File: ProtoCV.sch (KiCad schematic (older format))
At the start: 2 parts

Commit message: Draft schematic.
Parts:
- removed U?: DC80508Z, symbol Local:DC80508Z
- removed U?: IPS240x240, symbol Local:IPS240x240
- added C1, C10, C2, C3, C4, C7, C8, C9: 22p, symbol Device:C
- added C11, C12, C13, C15, C5, C6: 100n, symbol Device:C
- added C14: 1u, symbol Device:C
- added C16, C19, C20: 22u, Capacitor_SMD:C_1206_3216Metric, symbol Device:C
- added C17, C18: 22u, Capacitor_SMD:CP_Elec_5x5.4, symbol Device:CP
- added C21, C22, C23, C24, C27, C28: 100n, Capacitor_SMD:C_0603_1608Metric, symbol Device:C
- added C25, C26: 10u, Capacitor_SMD:CP_Elec_4x5.8, symbol Device:CP
- added D1, D2: DFLR1400-7, Diode_SMD:D_PowerDI-123, symbol Device:D
- added D3: LED, LED_SMD:LED_0603_1608Metric_Castellated, symbol Device:LED
- added FB1, FB2, FB3: Ferrite_Bead, Inductor_SMD:L_0603_1608Metric, symbol Device:Ferrite_Bead
- added H1, H2, H3, H4: MountingHole, symbol Mechanical:MountingHole
- added J1, J2, J3, J4, J5, J6, J7, J8: AudioJack2_SwitchT, symbol Connector:AudioJack2_SwitchT
- added J10: Conn_01x09_Male, symbol Connector:Conn_01x09_Male
- added J11: Conn_01x05_Male, symbol Connector:Conn_01x05_Male
- added J9: Conn_02x05_Odd_Even, Connector_PinHeader_2.54mm:PinHeader_2x05_P2.54mm_Vertical, symbol Connector_Generic:Conn_02x05_Odd_Even
- added L1: 33u, Inductor_SMD:L_0805_2012Metric, symbol pspice:INDUCTOR
- added R1, R13, R14, R15, R16, R2, R3, R4: 24k9, symbol Device:R
- added R10, R11, R12, R21, R22, R23, R24, R9: 220, symbol Device:R
- added R17, R18, R19, R20, R5, R6, R7, R8: 100k, symbol Device:R
- added R25, R26: 4k7, symbol Device:R
- added R27: 1k, Resistor_SMD:R_0603_1608Metric, symbol Device:R
- added U1, U2: OPA4192, symbol Amplifier_Operational:LM324A
- added U3: DC80508Z, symbol Local:DC80508Z
- added U4: R-78E3.3-0.5, Converter_DCDC:Converter_DCDC_RECOM_R-78E-0.5_THT, symbol Regulator_Switching:R-78E3.3-0.5
- added U5: LD2981ABU33TR, Package_TO_SOT_SMD:SOT-89-3, symbol Local:LD2981ABU33TR
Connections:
- net labels added: +12V, +3.3V, +3.3VA, -12V, BIAS, CV0, CV1, CV2, CV3, CV4, CV5, CV6, CV7, GND, OUT0, OUT1, OUT2, OUT3, OUT4, OUT5, OUT6, OUT7, VREF
- wire segments 0 -> 286
- no-connect marks 0 -> 8

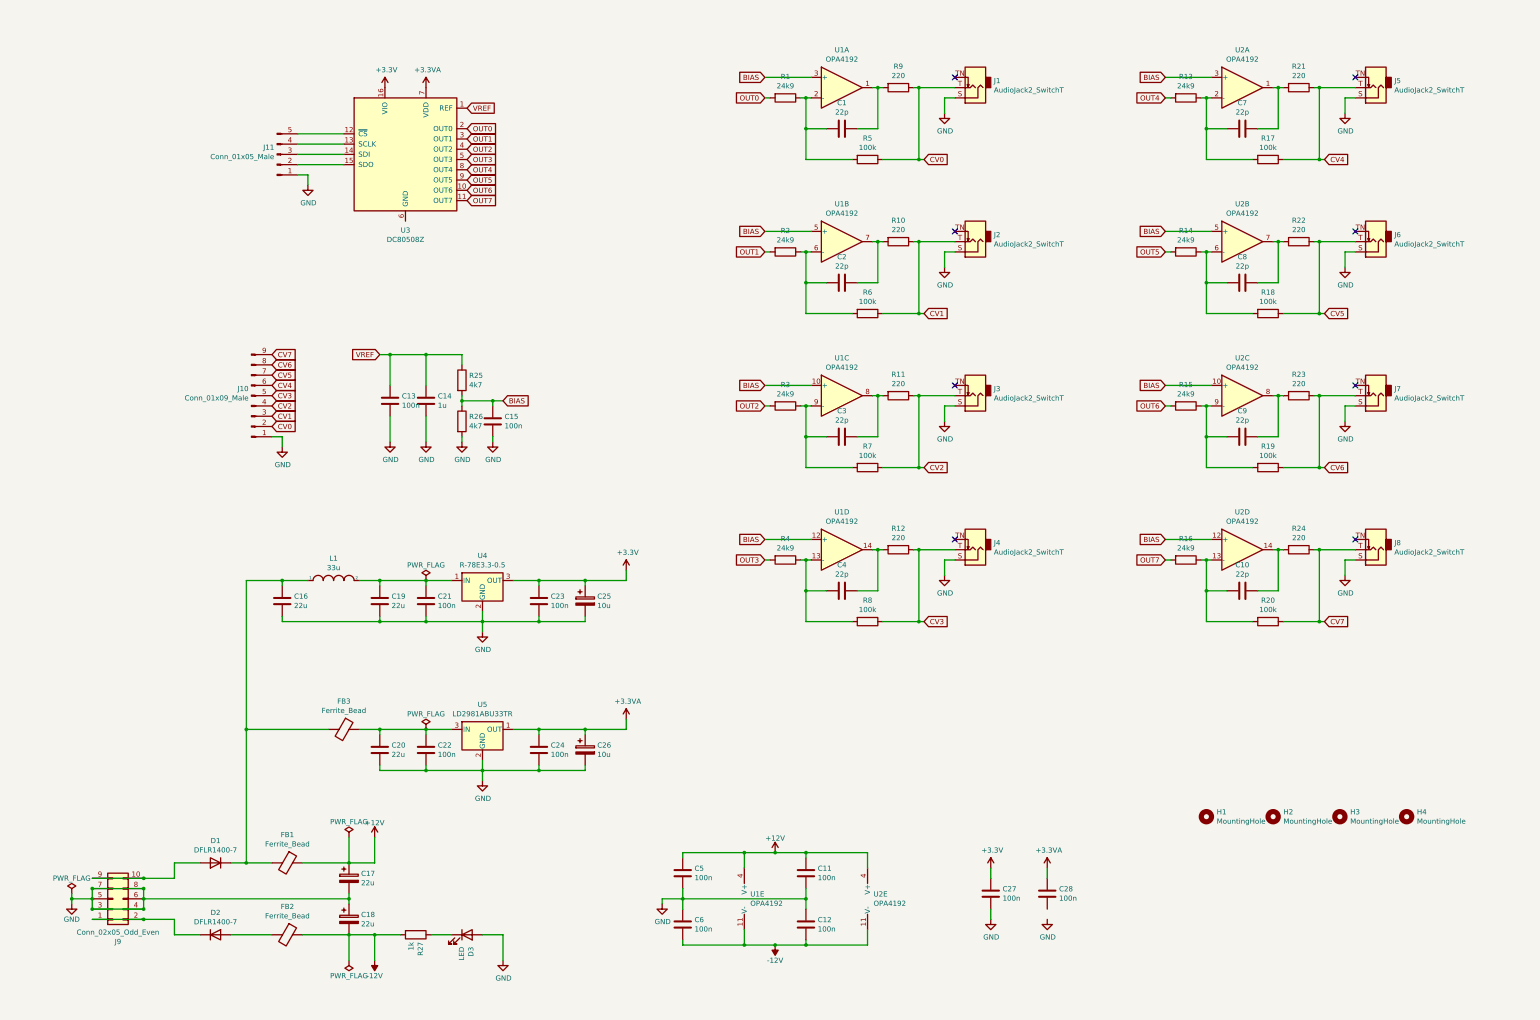
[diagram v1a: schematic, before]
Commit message: Added triggers.
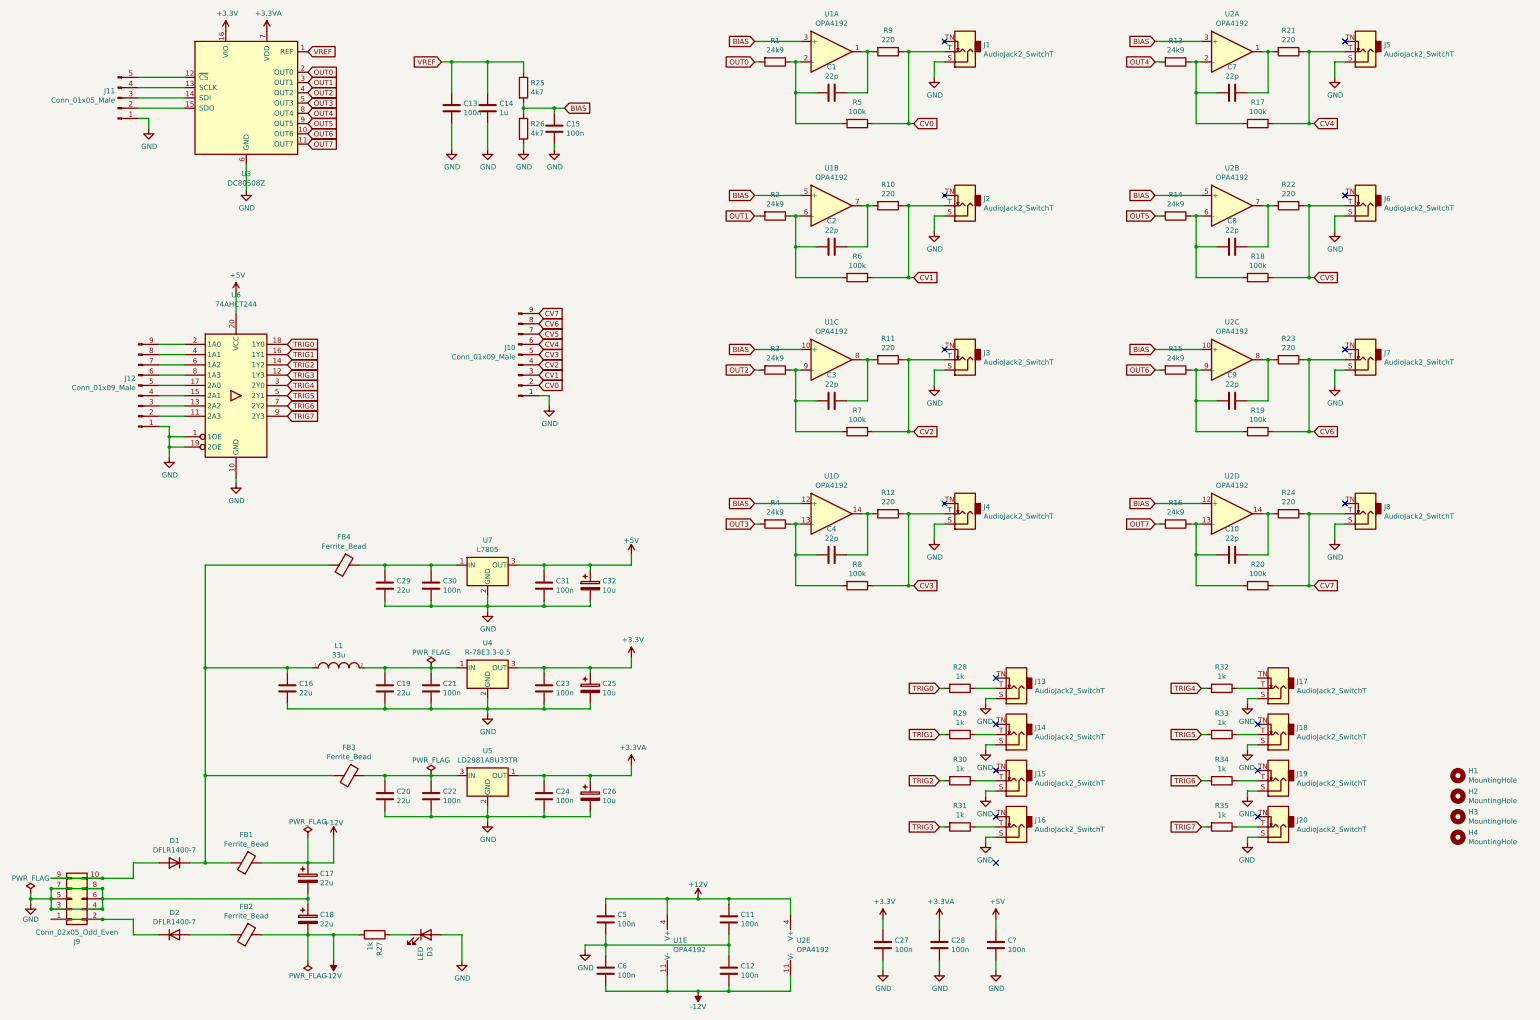
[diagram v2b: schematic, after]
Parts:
- added C29: 22u, Capacitor_SMD:C_1206_3216Metric, symbol Device:C
- added C30, C31, C?: 100n, Capacitor_SMD:C_0603_1608Metric, symbol Device:C
- added C32: 10u, Capacitor_SMD:CP_Elec_4x5.8, symbol Device:CP
- added FB4: Ferrite_Bead, Inductor_SMD:L_0603_1608Metric, symbol Device:Ferrite_Bead
- added J12: Conn_01x09_Male, symbol Connector:Conn_01x09_Male
- added J13, J14, J15, J16, J17, J18, J19, J20: AudioJack2_SwitchT, Local.pretty:PJ398SM, symbol Connector:AudioJack2_SwitchT
- added R28, R29, R30, R31, R32, R33, R34, R35: 1k, Resistor_SMD:R_0603_1608Metric, symbol Device:R
- added U6: 74AHCT244, Package_SO:TSSOP-20_4.4x6.5mm_P0.65mm, symbol 74xx:74HCT244
- added U7: L7805, Package_TO_SOT_SMD:SOT-223-3_TabPin2, symbol Regulator_Linear:L7805
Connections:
- net GND: now also C28.2, U3.6 (GND), C29.2, C30.2, C31.2, C32.2, C?.2, J12.1 (Pin_1), J13.S, J14.S, J15.S, J16.S, J17.S, J18.S, J19.S, J20.S, U6.1 (1OE), U6.10 (GND), U6.19 (2OE), U7.2 (GND)
- net at C16.1, D1.1 (K), FB1.2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: now also FB4.2
- new net: C29.1, C30.1, FB4.1, U7.1 (IN)
- new net: J13.T, R28.1
- new net: J12.2 (Pin_2), U6.11 (2A3)
- new net: J12.3 (Pin_3), U6.13 (2A2)
- new net: J12.4 (Pin_4), U6.15 (2A1)
- new net: J12.5 (Pin_5), U6.17 (2A0)
- new net: J12.9 (Pin_9), U6.2 (1A0)
- new net: J12.8 (Pin_8), U6.4 (1A1)
- new net: J12.7 (Pin_7), U6.6 (1A2)
- new net: J12.6 (Pin_6), U6.8 (1A3)
- new net: J14.T, R29.1
- new net: J15.T, R30.1
- new net: J16.T, R31.1
- new net: J17.T, R32.1
- new net: J18.T, R33.1
- new net: J19.T, R34.1
- new net: J20.T, R35.1
- new net +5V: C31.1, C32.1, C?.1, U6.20 (VCC), U7.3 (OUT)
- new net TRIG0: R28.2, U6.18 (1Y0)
- new net TRIG1: R29.2, U6.16 (1Y1)
- new net TRIG2: R30.2, U6.14 (1Y2)
- new net TRIG3: R31.2, U6.12 (1Y3)
- new net TRIG4: R32.2, U6.3 (2Y0)
- new net TRIG5: R33.2, U6.5 (2Y1)
- new net TRIG6: R34.2, U6.7 (2Y2)
- new net TRIG7: R35.2, U6.9 (2Y3)
- no-connect marks 8 -> 16
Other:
- moved on the sheet: C1, C10, C11, C12, C13, C14, C15, C16, C17, C18, C19, C2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
